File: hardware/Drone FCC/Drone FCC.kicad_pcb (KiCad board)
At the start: 4 copper layers, 60 x 100 mm, 167 parts, among them J1 UARTs externo x 3, J1001 SPI externo, J1003 I2C externo x2, J1005 5V y 3V3 x 2, J201 Mag Dupont, J202 Mag DF13, J203 GPS Dupont, J204 GPS M8N - DF13, J301 ESC 1, J302 ESC 2, J303 ESC 3, J304 ESC 4, J305 ESC 5, J306 ESC 6, J307 ESC 7, J308 ESC 8, J309 SERVO 1, J310 SERVO 2, J311 SERVO 3, J312 SERVO 4, J313 Power Servo, J401 DSM Spektrum JST, J402 PPM Dupont, J501 Micro USB - B, J601 SWD Debug Connector, J701 DM3AT-SF-PEJM5, J801 CAN 1 Connector 1, J803 CAN 2 Connector 1, J901 PM02 PixHawk, Q1101 2N7002, Q1102 2N7002, Q1103 2N7002, Q1104 2N7002, Q1105 2N7002, Q1106 2N7002, Q1107 2N7002, Q1108 2N7002, Q901 Q_PMOS_GSD, SW101 SW RESET, SW1101 SW Propósito General, SW1102 SW Propósito General, U101 STM32F746ZGTx, U201 ICM-42688-V, U202 ILPS22QSTR, U501 USBLC6-2SC6, U801 SN65HVD230, U802 SN65HVD230, U901 ZLDO1117QG33TA, Y101 12MHz, Y102 32.768kHz

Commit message: todo: route SWD connector
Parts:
- moved U202 296.1 mm to (150.2, 114.3), turned to -90 degrees
- moved J601 131.5 mm to (106.6, 70.3)
- moved J401 53.3 mm to (160.0, 114.8)
- moved J1003 48.3 mm to (175.5, 110.1), turned to 0 degrees
- moved J201 47.8 mm to (128.9, 121.0), turned to 180 degrees
- moved J203 46.7 mm to (128.9, 113.4), turned to 180 degrees
- moved J204 37.7 mm to (135.6, 107.0), turned to -90 degrees
- moved J202 32.8 mm to (137.2, 122.3), turned to -90 degrees
- moved U901 17.2 mm to (156.1, 126.9), turned to -90 degrees
- moved R906 11.6 mm to (143.0, 104.4)
- moved R907 11.5 mm to (144.4, 104.3)
- moved J1001 4.85 mm to (128.9, 105.9)
- moved D903 3.89 mm to (131.8, 125.9), turned to -90 degrees
- moved C117 3.43 mm to (161.5, 100.1), turned to 0 degrees
- moved J313 2.74 mm to (177.6, 129.4)
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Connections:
- J1003 pad 1: 5V -> /Conexiones_extra/I2CA_SDA
- J1003 pad 10: /Conexiones_extra/I2CA_SCL -> 3V3
- J1003 pad 2: 3V3 -> /Conexiones_extra/I2CA_SDA
- J1003 pad 3: 5V -> /Conexiones_extra/I2CA_SCL
- J1003 pad 4: 3V3 -> /Conexiones_extra/I2CA_SCL
- J1003 pad 7: /Conexiones_extra/I2CA_SDA -> 5V
- J1003 pad 8: /Conexiones_extra/I2CA_SDA -> 3V3
- J1003 pad 9: /Conexiones_extra/I2CA_SCL -> 5V
- J201 pad 1: /Sensores/MAG_INT_DATA_RDY -> /Sensores/GNSS_SDA
- J201 pad 2: GND -> unconnected-(J201-Pad2)
- J201 pad 3: /Sensores/GNSS_SDA -> /Sensores/GNSS_SCL
- J201 pad 5: /Sensores/GNSS_SCL -> /Sensores/MAG_INT_DATA_RDY
- J201 pad 6: unconnected-(J201-Pad6) -> GND
- J401 pad 3: /RC control/DSM_DATA -> /MCU/USART3_RX
- R103 pad 1: /Conexiones_extra/I2CA_SCL -> /Sensores/GNSS_SCL
- R104 pad 1: /Conexiones_extra/I2CA_SDA -> /Sensores/GNSS_SDA
- R105 pad 2: /Sensores/GNSS_SDA -> /Conexiones_extra/I2CA_SDA
- R106 pad 2: /Sensores/GNSS_SCL -> /Conexiones_extra/I2CA_SCL
- U101 pad 34: unconnected-(U101-Pad34) -> /Sensores/GNSS_Tx
- U101 pad 35: /Alimentación/I_MEAS -> /Sensores/GNSS_Rx
- U101 pad 36: /Alimentación/V_MEAS -> unconnected-(U101-Pad36)
- U101 pad 40: unconnected-(U101-Pad40) -> /Alimentación/I_MEAS
- U101 pad 41: /Sensores/GNSS_PPS -> /Alimentación/V_MEAS
- U101 pad 54: /Conexiones_extra/I2CA_SCL -> /Sensores/GNSS_SCL
- U101 pad 55: /Conexiones_extra/I2CA_SDA -> /Sensores/GNSS_SDA
- U101 pad 56: unconnected-(U101-Pad56) -> /Sensores/MAG_INT_DATA_RDY
- U101 pad 57: /Sensores/MAG_INT_DATA_RDY -> /MCU/PG_1(EXTI1)
- U101 pad 58: /Sensores/GNSS_Rx -> /MCU/UART7_RX
- U101 pad 59: /Sensores/GNSS_Tx -> /MCU/UART7_TX
- U101 pad 69: /Sensores/GNSS_SCL -> /Conexiones_extra/I2CA_SCL
- U101 pad 70: /Sensores/GNSS_SDA -> /Conexiones_extra/I2CA_SDA
- U101 pad 77: /Conexiones_extra/UARTA_TX -> /MCU/USART3_TX
- U101 pad 78: /Conexiones_extra/UARTA_RX -> /MCU/USART3_RX
- U201 pad 4: /MCU/PG_2(EXTI2) -> /MCU/PG_1(EXTI1)
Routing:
- net /Sensores/GNSS_SDA: track 20.5 -> 71.5 mm
- net /Sensores/GNSS_Rx: track 1.73 -> 39.7 mm, vias 1 -> 2
- net /Sensores/MAG_INT_DATA_RDY: track 0.00 -> 37.2 mm, vias 0 -> 1
- net /Sensores/GNSS_SCL: track 21.9 -> 56.9 mm
- net /MCU/USART3_RX: track 0.00 -> 34.3 mm
- net /Sensores/GNSS_Tx: track 1.73 -> 33.4 mm, vias 1 -> 2
- net /MCU/TIM4_CH4: track 9.64 -> 38.9 mm, vias 0 -> 1
- net /MCU/TIM4_CH3: track 9.30 -> 35.4 mm, vias 0 -> 1
- net /MCU/TIM4_CH2: track 7.39 -> 32.8 mm, vias 0 -> 1
- net /Sensores/GNSS_PPS: track 45.6 -> 21.1 mm, vias 2 -> 1
- net /MCU/TIM4_CH1: track 7.86 -> 29.3 mm, vias 0 -> 1
- net /MCU/SPI2_CS: track 4.94 -> 24.2 mm, vias 0 -> 2
- net /MCU/SPI2_MOSI: track 10.2 -> 26.4 mm, vias 1 -> 2
- net /MCU/SPI2_MISO: track 10.4 -> 26.3 mm, vias 1 -> 2
- net /MCU/TIM1_CH2: track 43.2 -> 32.7 mm
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
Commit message: included SWD header in routing
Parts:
- J701: moved to B.Cu
- moved SW101 262.3 mm to (127.7, 69.6), turned to -90 degrees
- moved SW1101 222.3 mm to (176.9, 56.0)
- moved SW1102 212.5 mm to (166.6, 51.4)
- moved J601 24.8 mm to (126.7, 55.8)
- moved J313 14.3 mm to (169.2, 141.0), turned to 0 degrees
- moved J309 8.04 mm to (153.9, 144.0)
- moved J310 8.04 mm to (156.4, 144.0)
- moved J311 8.04 mm to (158.9, 144.0)
- moved J312 8.04 mm to (161.5, 144.0)
- moved J301 5.79 mm to (131.7, 144.1)
- moved J302 5.79 mm to (134.3, 144.1)
- moved J303 5.79 mm to (136.8, 144.1)
- moved J304 5.79 mm to (139.3, 144.1)
- moved J305 5.79 mm to (141.9, 144.1)
- moved J306 5.79 mm to (144.4, 144.1)
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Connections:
- U101 pad 36: unconnected-(U101-Pad36) -> /Sensores/GNSS_PPS
- U101 pad 58: /MCU/UART7_RX -> /Conexiones_extra/UARTA_RX
- U101 pad 59: /MCU/UART7_TX -> /Conexiones_extra/UARTA_TX
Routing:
- net /Debug/SWDIO: track 0.00 -> 48.4 mm, vias 0 -> 1
- net /Debug/NRST: track 0.00 -> 48.3 mm, vias 0 -> 2
- net /Debug/SWCLK: track 0.00 -> 44.8 mm, vias 0 -> 1
- net /MCU/TIM4_CH1: track 29.3 -> 72.3 mm
- net /Conexiones_extra/UARTA_TX: track 0.00 -> 28.3 mm, vias 0 -> 1
- net /Conexiones_extra/UARTA_RX: track 0.00 -> 27.1 mm, vias 0 -> 1
- net /Debug/SWO: track 1.39 -> 27.7 mm, vias 0 -> 1
- net /MCU/TIM1_CH1: track 35.4 -> 9.37 mm
- net /Conexiones_extra/UARTB_TX: track 16.9 -> 42.8 mm, vias 0 -> 1
- net /Sensores/GNSS_PPS: track 21.1 -> 40.1 mm, vias 1 -> 2
- net /Conexiones_extra/UARTB_RX: track 21.2 -> 37.8 mm
- net /Conexiones_extra/UARTC_TX: track 19.2 -> 34.6 mm
- net Net-(R803-Pad2): track 14.8 -> 2.12 mm, vias 2 -> 1
- net /Conexiones_extra/UARTC_RX: track 21.5 -> 32.5 mm
- net /Conexiones_extra/SPI_EOC: track 15.6 -> 5.76 mm
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
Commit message: added LEDs in routing
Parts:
- J701: moved to F.Cu
- Q1101, Q1102, Q1103, Q1104, Q1105, Q1106, Q1107, Q1108, R103, R104, R105, R106, R107, R108, R109, R110, R1101, R1102, R1104, R1105, R1107, R1108, R111, R1110, R1111, R1113, R1114, R1115, R1116, R1117, R1118, R1119, R112, R1120, R1122, R1123, R1124, R1125, R1126, R703, R704, R705, R706: moved to B.Cu
- moved C204 310.3 mm to (151.8, 112.1), turned to 180 degrees
- moved C205 309.1 mm to (153.5, 114.4), turned to -90 degrees
- moved R106 302.2 mm to (164.9, 109.3), turned to 90 degrees
- moved C206 300.8 mm to (155.2, 114.4), turned to -90 degrees
- moved R105 299.7 mm to (166.6, 107.3), turned to -90 degrees
- moved R103 299.2 mm to (153.0, 101.9), turned to 180 degrees
- moved C203 285.4 mm to (151.0, 110.4), turned to 180 degrees
- moved R104 284.0 mm to (155.2, 103.7)
- moved C201 277.7 mm to (149.6, 105.0), turned to -90 degrees
- moved C702 273.9 mm to (165.7, 66.6), turned to -90 degrees
- moved R701 271.8 mm to (188.9, 54.0)
- moved C119 264.0 mm to (125.7, 84.5), turned to 180 degrees
- moved R705 262.6 mm to (172.1, 66.6)
- moved R706 260.2 mm to (169.7, 68.5), turned to 180 degrees
- moved R704 256.7 mm to (163.1, 64.7), turned to 180 degrees
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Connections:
- J1001 pad 7: /Conexiones_extra/SPI_MISO -> /Conexiones_extra/SPI_MOSI
- J1001 pad 8: /Conexiones_extra/SPI_MOSI -> /Conexiones_extra/SPI_MISO
- U101 pad 1: unconnected-(U101-Pad1) -> /Interfaz_CAN/CAN1_MODE
- U101 pad 10: unconnected-(U101-Pad10) -> /MCU/PF0
- U101 pad 11: unconnected-(U101-Pad11) -> /MCU/PF1
- U101 pad 12: unconnected-(U101-Pad12) -> /Leds indicadores + pulsadores/LED4
- U101 pad 13: unconnected-(U101-Pad13) -> /Leds indicadores + pulsadores/SW_1
- U101 pad 134: /Interfaz_CAN/CAN2_MODE -> /Leds indicadores + pulsadores/LED6
- U101 pad 137: /Interfaz_CAN/CAN1_MODE -> /Interfaz_CAN/CAN2_MODE
- U101 pad 14: unconnected-(U101-Pad14) -> /Leds indicadores + pulsadores/SW_2
- U101 pad 141: /MCU/UART8_RX -> /Leds indicadores + pulsadores/LED5
- U101 pad 142: /MCU/UART8_TX -> /Leds indicadores + pulsadores/LED8
- U101 pad 2: unconnected-(U101-Pad2) -> /Leds indicadores + pulsadores/LED1
- U101 pad 3: unconnected-(U101-Pad3) -> /Leds indicadores + pulsadores/LED2
- U101 pad 37: /MCU/TIM2_CH4 -> /Alimentación/I_MEAS
- U101 pad 4: /MCU/TIM9_CH1 -> /Leds indicadores + pulsadores/LED7
- U101 pad 40: /Alimentación/I_MEAS -> /MCU/ADC1_IN4
- U101 pad 48: unconnected-(U101-Pad48) -> /Sensores/MAG_INT_DATA_RDY
- U101 pad 5: unconnected-(U101-Pad5) -> /Leds indicadores + pulsadores/LED3
- U101 pad 50: unconnected-(U101-Pad50) -> /MCU/PF12(EXTI12)
- U101 pad 56: /Sensores/MAG_INT_DATA_RDY -> /MCU/PG_0(EXTI0)
- U201 pad 4: /MCU/PG_1(EXTI1) -> /MCU/PF12(EXTI12)
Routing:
- net GND: track 68.3 -> 114.3 mm, vias 18 -> 47
- net /MCU/PD_4(EXTI4): track 0.00 -> 44.6 mm, vias 0 -> 1
- net /MCU/TIM1_CH1: track 9.37 -> 46.4 mm
- net /Leds indicadores + pulsadores/LED1: track 0.00 -> 34.4 mm, vias 0 -> 1
- net 3V3: track 62.6 -> 95.6 mm, vias 10 -> 30
- net /Leds indicadores + pulsadores/LED2: track 0.00 -> 31.2 mm, vias 0 -> 1
- net /Leds indicadores + pulsadores/LED7: track 0.00 -> 30.4 mm, vias 0 -> 1
- net /MCU/TIM4_CH2: track 30.7 -> 61.0 mm
- net /MCU/TIM4_CH3: track 33.2 -> 63.2 mm
- net /MCU/TIM4_CH4: track 34.6 -> 62.4 mm
- net /Leds indicadores + pulsadores/SW_2: track 0.00 -> 26.9 mm, vias 0 -> 1
- net /Conexiones_extra/SPI_EOC: track 5.76 -> 31.6 mm
- net /Debug/SWCLK: track 44.8 -> 19.6 mm, vias 1 -> 0
- net /Debug/SWDIO: track 48.4 -> 23.2 mm
- net /Leds indicadores + pulsadores/LED3: track 0.00 -> 23.9 mm, vias 0 -> 1
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
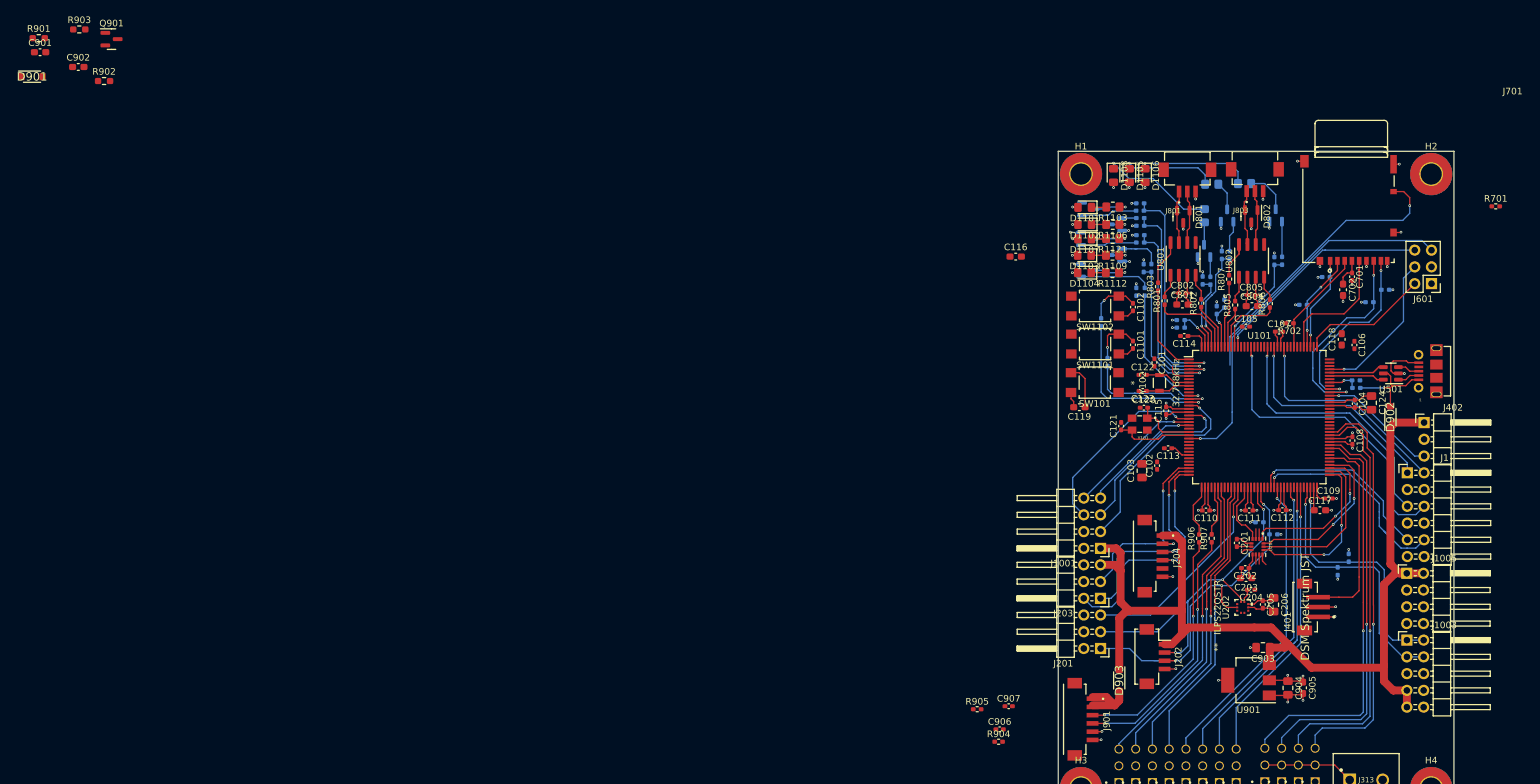
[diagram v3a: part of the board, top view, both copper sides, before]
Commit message: included all components on PCB
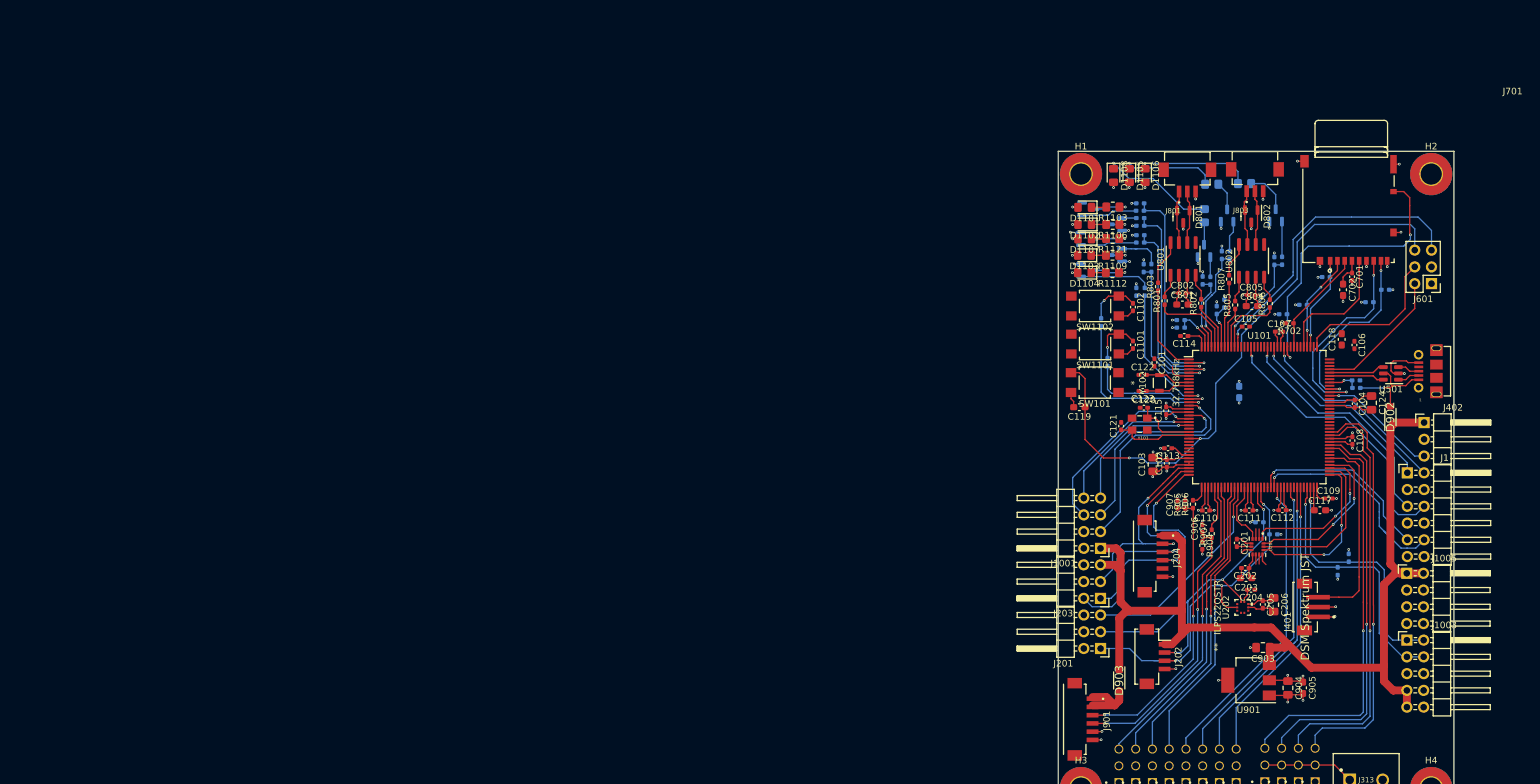
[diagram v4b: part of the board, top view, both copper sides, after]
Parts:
- removed C901: 1.6u, Capacitor_SMD:C_0603_1608Metric_Pad1.08x0.95mm_HandSolder
- removed C902: 0.1u, Capacitor_SMD:C_0603_1608Metric_Pad1.08x0.95mm_HandSolder
- removed D901: PMEG60T30ELRX, PMEG60T30ELRX:SODFL3517X110N
- removed Q901: Q_PMOS_GSD, Package_TO_SOT_SMD:SOT-23
- removed R901: 10, Resistor_SMD:R_0603_1608Metric_Pad0.98x0.95mm_HandSolder
- removed R902: 6.8k, Resistor_SMD:R_0603_1608Metric_Pad0.98x0.95mm_HandSolder
- removed R903: 33, Resistor_SMD:R_0603_1608Metric_Pad0.98x0.95mm_HandSolder
- C116, R701: moved to B.Cu
- moved R905 44.3 mm to (141.8, 99.2), turned to 90 degrees
- moved C906 43.3 mm to (144.4, 102.9), turned to 90 degrees
- moved R904 42.9 mm to (144.4, 105.4), turned to -90 degrees
- moved C907 39.9 mm to (140.6, 99.2), turned to 90 degrees
- moved C116 39.6 mm to (150.0, 82.1), turned to 90 degrees
- moved R701 36.2 mm to (156.6, 70.4), turned to 180 degrees
- moved R906 5.28 mm to (143.0, 99.2)
- moved C103 1.92 mm to (136.9, 93.1)
- moved C102 1.51 mm to (139.0, 93.0)
- moved R907 0.70 mm to (145.8, 103.6)
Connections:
- J601 pad 2: /Debug/SWCLK -> /Debug/SWDIO
- J601 pad 4: /Debug/SWDIO -> /Debug/SWCLK
- J601 pad 5: /Debug/NRST -> /Debug/SWO
- J601 pad 6: /Debug/SWO -> /Debug/NRST
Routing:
- net /Debug/NRST: track 64.2 -> 93.0 mm, vias 1 -> 2
- net /Debug/SWO: track 33.9 -> 45.9 mm
- net GND: track 114.3 -> 125.3 mm, vias 47 -> 55
- net 3V3: track 95.6 -> 104.9 mm, vias 30 -> 34
- net Net-(C907-Pad1): track 36.9 -> 44.1 mm
- net /Alimentación/I_MEAS: track 8.03 -> 2.87 mm
- net /Sensores/GNSS_Rx: track 34.2 -> 38.9 mm
- net /Conexiones_extra/UARTB_TX: track 46.7 -> 42.5 mm
- net /Debug/SWCLK: track 19.6 -> 23.5 mm
- net /Sensores/GNSS_PPS: track 37.8 -> 41.7 mm
- net /Conexiones_extra/UARTB_RX: track 39.6 -> 35.9 mm
- net Net-(C906-Pad1): track 38.7 -> 42.2 mm
- net /Conexiones_extra/UARTC_RX: track 33.6 -> 30.1 mm
- net /Conexiones_extra/UARTC_TX: track 33.5 -> 30.3 mm
- net /Conexiones_extra/SPI_MOSI: track 18.6 -> 21.5 mm
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
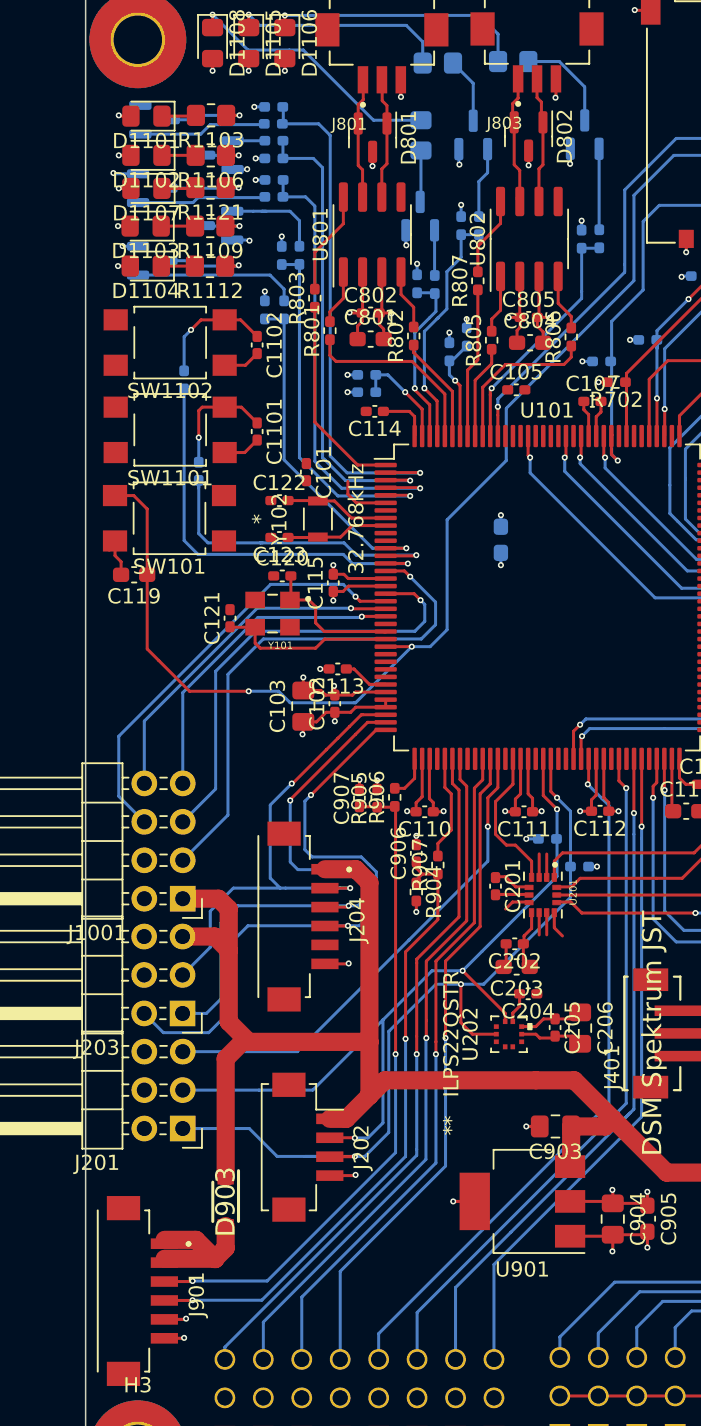
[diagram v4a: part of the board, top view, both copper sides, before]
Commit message: add 3D models to footprints
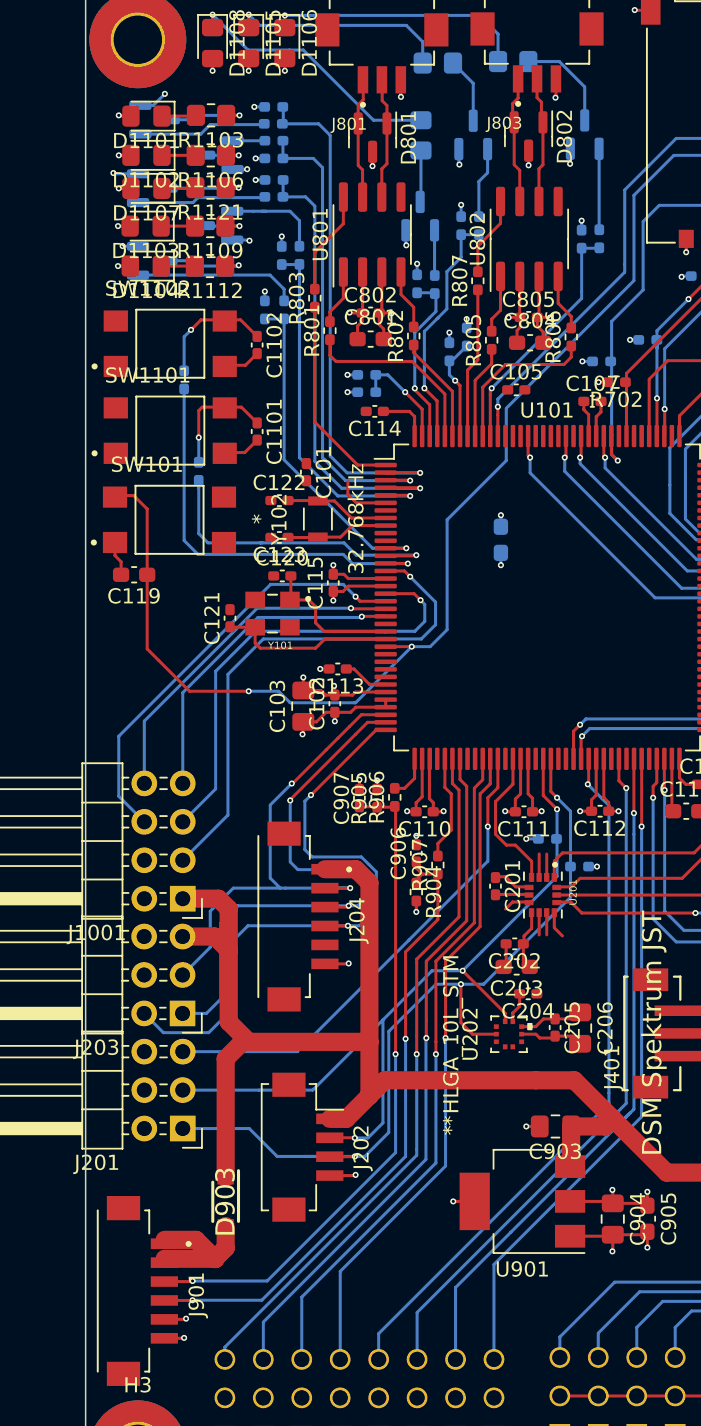
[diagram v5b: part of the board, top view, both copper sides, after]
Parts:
- SW101: footprint Button_Switch_SMD:SW_SPST_TL3305A -> TL3305AF160QG:SW_TL3305AF160QG
- SW1101, SW1102: value SW Propósito General -> SW Proposito General; footprint Button_Switch_SMD:SW_SPST_TL3305A -> TL3305AF160QG:SW_TL3305AF160QG
- U202: value ILPS22QSTR -> HLGA_10L_STM
- moved SW101 0.10 mm to (128.1, 80.8), turned to 0 degrees
- moved SW1102 0.08 mm to (128.1, 69.2), turned to 0 degrees
- moved SW1101 0.05 mm to (128.1, 74.9), turned to 0 degrees
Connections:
- SW101 pad 2: /Debug/NRST -> GND
- SW1101 pad 2: Net-(C1101-Pad1) -> GND
- SW1102 pad 2: Net-(C1102-Pad1) -> GND
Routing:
- net GND: track 125.3 -> 127.3 mm, vias 55 -> 56
- added copper zone on In2.Cu, net 3V3
- added copper zone on In1.Cu, net GND
